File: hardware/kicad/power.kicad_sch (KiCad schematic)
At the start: 82 parts, among them IC401 TPS51206DSQR, U401 TPS62130ARGTR, U402 TPS62130ARGTR, U404 SPX3819M5-L-3-3, U405 TPS62130ARGTR

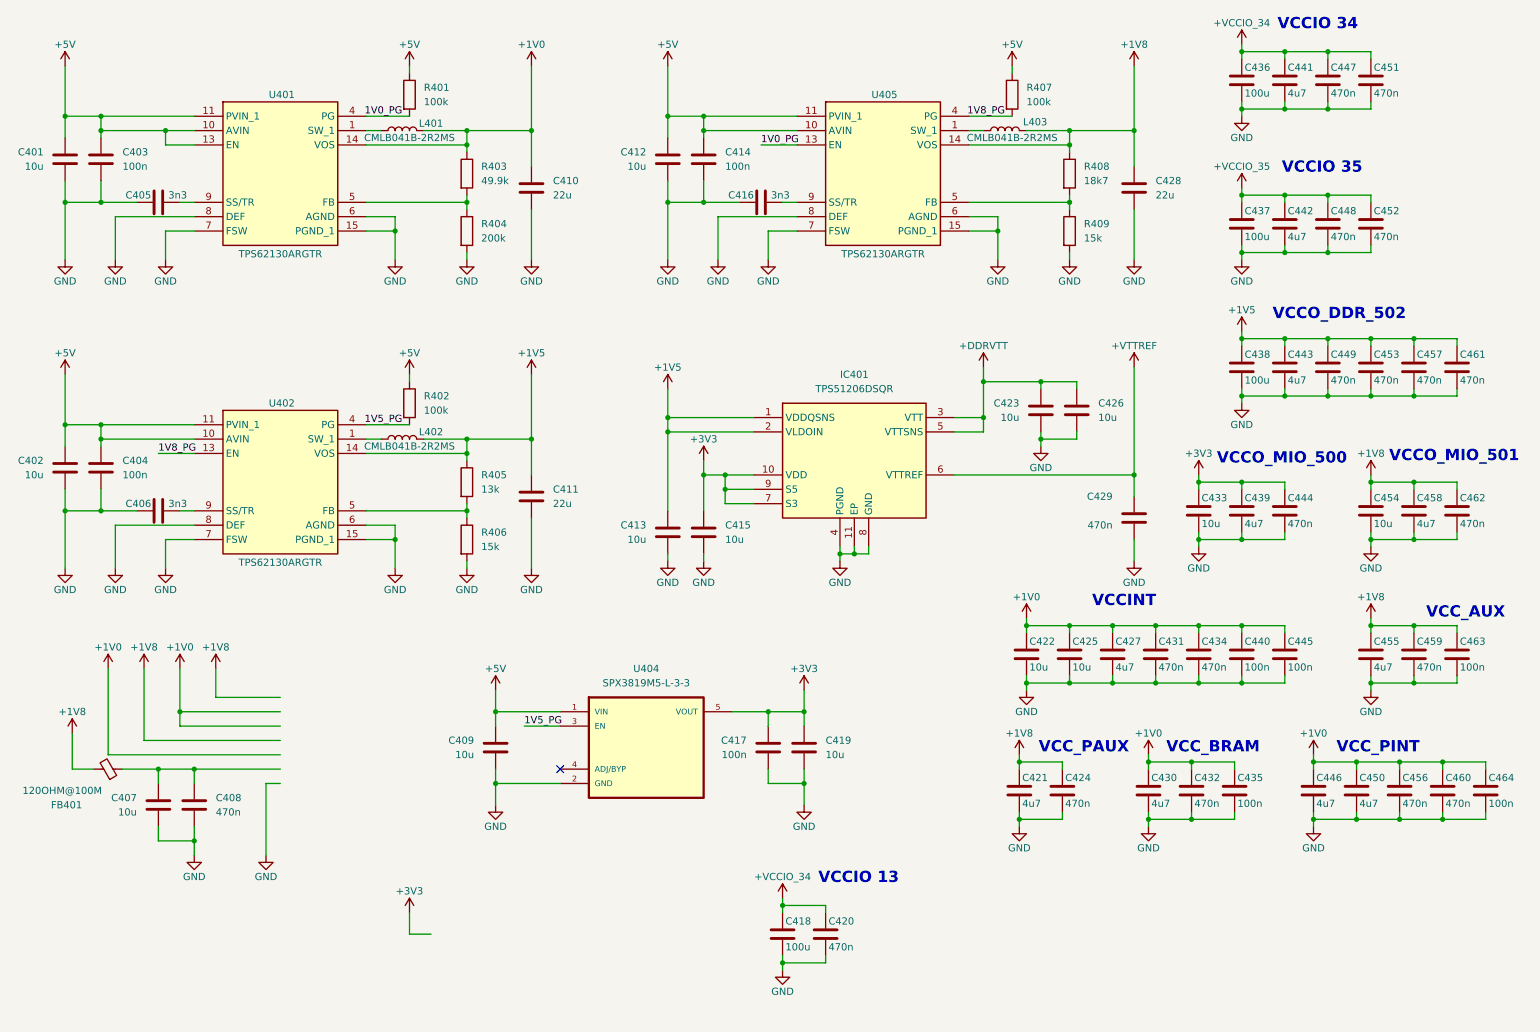
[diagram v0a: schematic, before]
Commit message: layout: finish dq0 & dq1 routing
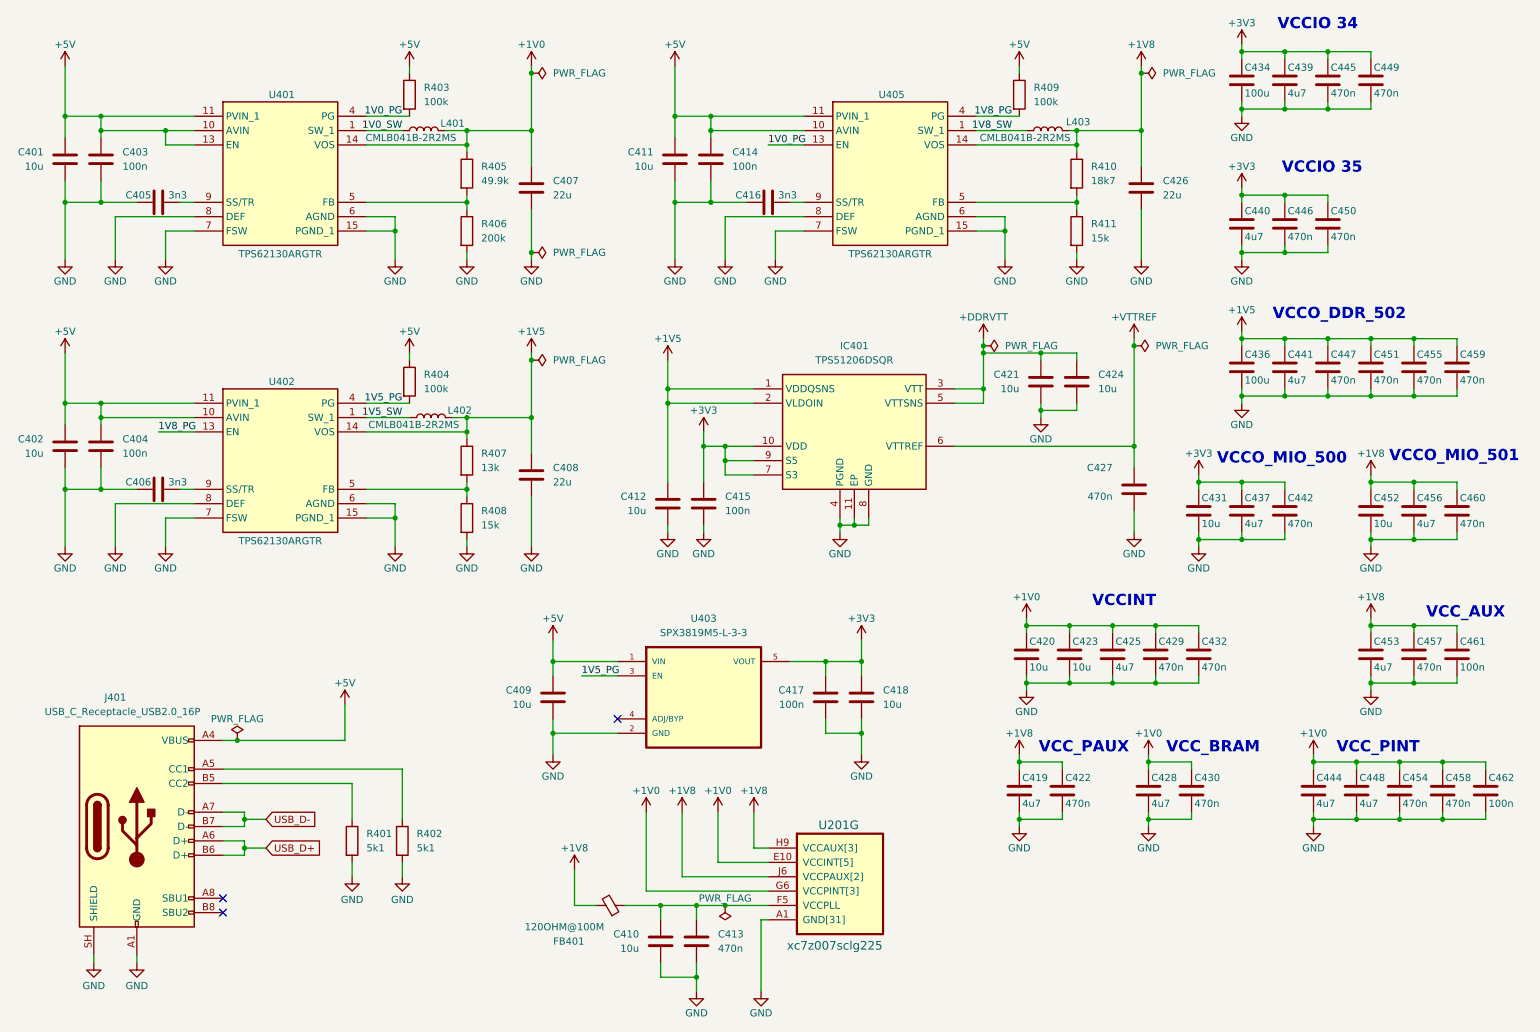
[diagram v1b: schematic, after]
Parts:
- removed C407: 10u, Capacitor_SMD:C_0805_2012Metric, symbol Device:C
- removed C408, C420: 470n, Capacitor_SMD:C_0402_1005Metric, symbol Device:C
- removed C418, C437: 100u, Capacitor_SMD:C_1206_3216Metric, symbol Device:C
- removed C435, C440, C445: 100n, Capacitor_SMD:C_0402_1005Metric, symbol Device:C
- added C410: 10u, Capacitor_SMD:C_0603_1608Metric, symbol Device:C
- added C413: 470n, Capacitor_SMD:C_0402_1005Metric, symbol Device:C
- added J401: USB_C_Receptacle_USB2.0_16P, Connector_USB:USB_C_Receptacle_GCT_USB4105-xx-A_16P_TopMnt_Horizontal, symbol Connector:USB_C_Receptacle_USB2.0_16P
- added R401, R402: 5k1, Resistor_SMD:R_0402_1005Metric, symbol Device:R
- added U201: xc7z007sclg225, Package_BGA:Xilinx_CLG225, symbol Xilinx7:xc7z007sclg225
- C415: value 10u -> 100n; footprint Capacitor_SMD:C_0805_2012Metric -> Capacitor_SMD:C_0402_1005Metric
- U403: renamed from U404; PACKAGE (none) -> SOT-23-5
- renumbered C410 to C407, C411 to C408, C412 to C411, C413 to C412, C419 to C418, C421 to C419, C422 to C420, C423 to C421, C424 to C422, C425 to C423, C426 to C424, C427 to C425, C428 to C426, C429 to C427, C430 to C428, C431 to C429, C432 to C430, C433 to C431, C434 to C432, C436 to C434, C438 to C436, C439 to C437, C441 to C439, C442 to C440, C443 to C441, C444 to C442, C446 to C444, C447 to C445, C448 to C446, C449 to C447, C450 to C448, C451 to C449, C452 to C450, C453 to C451, C454 to C452, C455 to C453, C456 to C454, C457 to C455, C458 to C456, C459 to C457, C460 to C458, C461 to C459, C462 to C460, C463 to C461, C464 to C462, R401 to R403, R402 to R404, R403 to R405, R404 to R406, R405 to R407, R406 to R408, R407 to R409, R408 to R410, R409 to R411
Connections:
- net +VCCIO_34 is gone; now on net +3V3: C434.1, C439.1, C445.1, C449.1
- net +VCCIO_35 is gone; now on net +3V3: C440.1, C446.1, C450.1
- net +1V0: now also U201.E10 (VCCINT[5]), U201.F9 (VCCINT[5]), U201.G10 (VCCINT[5]), U201.G6 (VCCPINT[3]), U201.H5 (VCCPINT[3]), U201.J10 (VCCINT[5]), U201.K5 (VCCPINT[3]), U201.L10 (VCCINT[5])
- net +1V8: now also U201.H9 (VCCAUX[3]), U201.J6 (VCCPAUX[2]), U201.J8 (VCCAUX[3]), U201.K9 (VCCAUX[3]), U201.L6 (VCCPAUX[2])
- net +5V: now also J401.A4 (VBUS), J401.A9 (VBUS), J401.B4 (VBUS), J401.B9 (VBUS)
- net GND: now also C410.2, C413.2, J401.A1 (GND), J401.A12 (GND), J401.B1 (GND), J401.B12 (GND), J401.SH (SHIELD), R401.2, R402.2, U201.A1 (GND[31]), U201.A11 (GND[31]), U201.B8 (GND[31]), U201.C15 (GND[31]), U201.C5 (GND[31]), U201.D12 (GND[31]), U201.D2 (GND[31]), U201.E5 (GND[31]), U201.E7 (GND[31]), U201.E9 (GND[31]), U201.F10 (GND[31]), U201.G13 (GND[31]), U201.G3 (GND[31]), U201.G5 (GND[31]), U201.H10 (GND[31]), U201.H6 (GND[31]), U201.J5 (GND[31]), U201.J9 (GND[31]), U201.K10 (GND[31]), U201.K14 (GND[31]), U201.K4 (GND[31]), U201.K7 (GND[31]), U201.L1 (GND[31]), U201.L11 (GND[31]), U201.L5 (GND[31]), U201.M8 (GND[31]), U201.N15 (GND[31]), U201.N5 (GND[31]), U201.P12 (GND[31]), U201.P2 (GND[31]), U201.R9 (GND[31])
- net at FB401.1: now also C410.1, C413.1, U201.F5 (VCCPLL)
- net 1V0_SW: now reaches L401.1, U401.1 (SW_1), U401.2 (SW_2), U401.3 (SW_3)
- net 1V8_SW: now reaches L403.1, U405.1 (SW_1), U405.2 (SW_2), U405.3 (SW_3)
- net 1V5_SW: now reaches L402.1, U402.1 (SW_1), U402.2 (SW_2), U402.3 (SW_3)
- new net: J401.B5 (CC2), R401.1
- new net: J401.A5 (CC1), R402.1
- new net USB_D+: J401.A6 (D+), J401.B6 (D+)
- new net USB_D-: J401.A7 (D-), J401.B7 (D-)
- no-connect marks 1 -> 3
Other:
- note removed: "VCCIO 13"
- moved on the sheet: C402, C404, C406, C408, C409, C411, C412, C414, C415, C416, C417, C418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

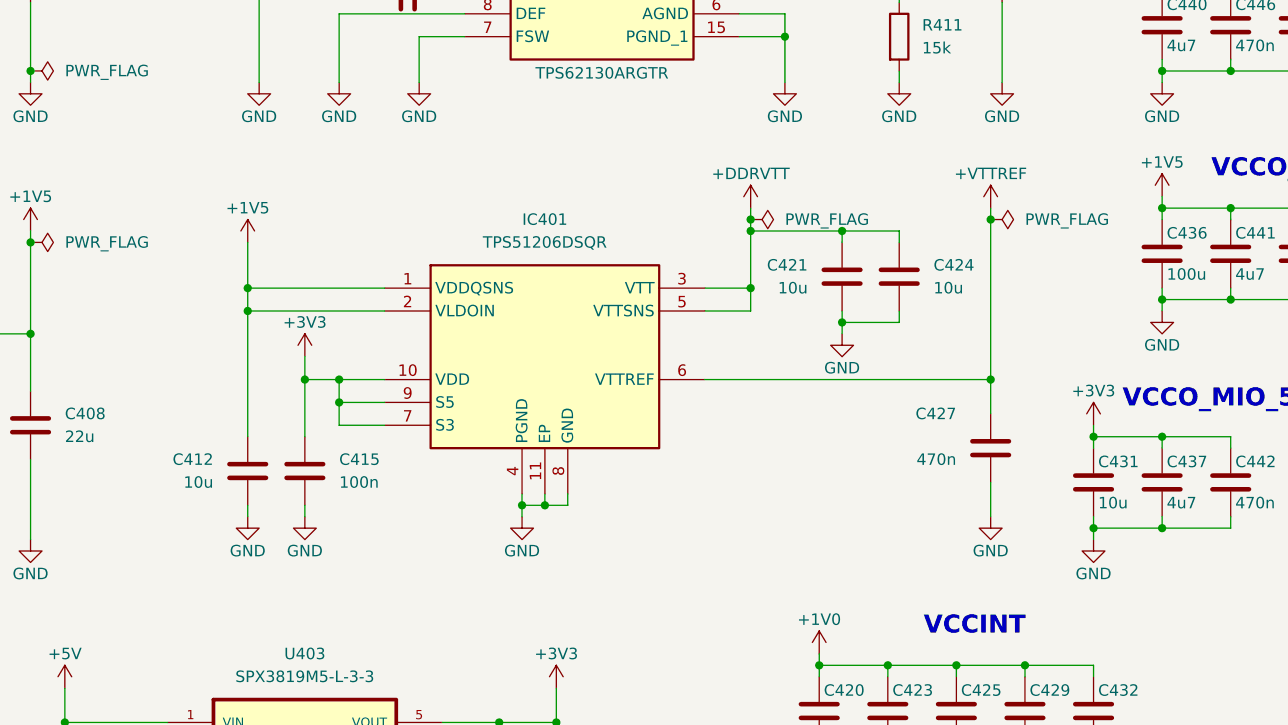
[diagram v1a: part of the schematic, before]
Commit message: pcb: complete FPGA and DDR BGA breakout
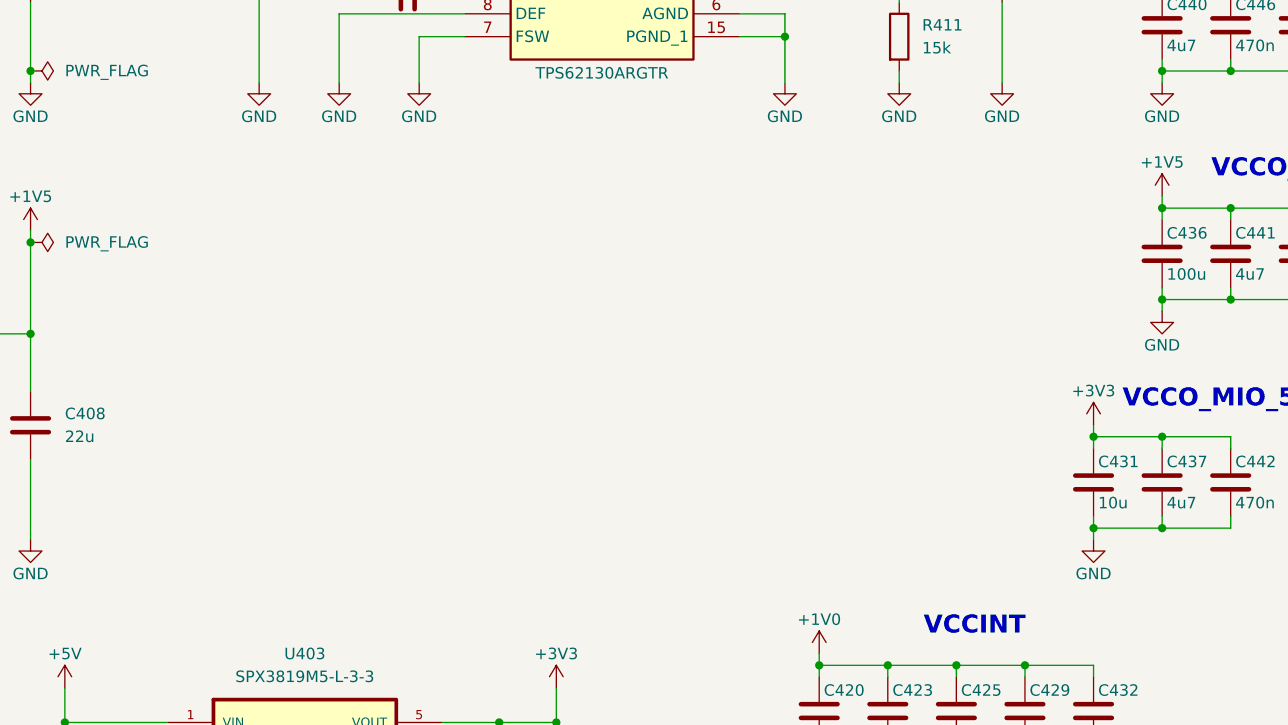
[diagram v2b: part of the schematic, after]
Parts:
- removed C412, C421, C424: 10u, Capacitor_SMD:C_0805_2012Metric, symbol Device:C
- removed C415: 100n, Capacitor_SMD:C_0402_1005Metric, symbol Device:C
- removed C427: 470n, Capacitor_SMD:C_0402_1005Metric, symbol Device:C
- removed IC401: TPS51206DSQR, Project:SON40P200X200X80-11N, symbol TPS51206DSQR:TPS51206DSQR

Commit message: feat: need switch two singals of SD inferface
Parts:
- C401, C402, C407, C408, C409, C411, C418, C420, C423, C426, C431, C452: footprint Capacitor_SMD:C_0805_2012Metric -> Capacitor_SMD:C_0603_1608Metric
- R401, R402: footprint Resistor_SMD:R_0402_1005Metric -> Resistor_SMD:R_0603_1608Metric
- U201: footprint Package_BGA:Xilinx_CLG225 -> (none)
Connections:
- net USB_D+: no longer names the net of J401.A6 (D+)
- net USB_D+: no longer J401.B6 (D+)
- net USB_D-: no longer names the net of J401.A7 (D-)
- net USB_D-: no longer J401.B7 (D-)
- no-connect marks 3 -> 7
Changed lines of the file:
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@@
 	)
 	(junction
-		(at 57.15 158.75)
-		(diameter 0)
-		(color 0 0 0 0)
-	)
-	(junction
 		(at 261.62 158.75)
 		(diameter 0)
@@
 	)
 	(junction
-		(at 57.15 163.83)
-		(diameter 0)
-		(color 0 0 0 0)
-	)
-	(junction
 		(at 31.75 49.53)
 		(diameter 0)
@@
 	)
 	(no_connect
+		(at 53.34 157.48)
+	)
+	(no_connect
 		(at 123.19 140.97)
 	)
@@
 	)
 	(no_connect
+		(at 53.34 160.02)
+	)
+	(no_connect
+		(at 53.34 165.1)
+	)
+	(no_connect
+		(at 53.34 162.56)
+	)
+	(no_connect
 		(at 53.34 172.72)
 	)
@@
 	(wire
 		(pts
-			(xy 57.15 163.83) (xy 60.96 163.83)
-		)
-		(stroke
-			(width 0)
-			(type default)
-		)
-	)
-	(wire
-		(pts
 			(xy 78.74 87.63) (xy 86.36 87.63)
 		)
@@
 	(wire
 		(pts
-			(xy 53.34 160.02) (xy 57.15 160.02)
-		)
-		(stroke
-			(width 0)
-			(type default)
-		)
-	)
-	(wire
-		(pts
 			(xy 130.81 184.15) (xy 130.81 186.69)
 		)
@@
 	(wire
 		(pts
-			(xy 57.15 158.75) (xy 57.15 160.02)
-		)
-		(stroke
-			(width 0)
-			(type default)
-		)
-	)
-	(wire
-		(pts
 			(xy 96.52 87.63) (xy 96.52 90.17)
 		)
@@
 	(wire
 		(pts
-			(xy 57.15 162.56) (xy 57.15 163.83)
-		)
-		(stroke
-			(width 0)
-			(type default)
-		)
-	)
-	(wire
-		(pts
 			(xy 78.74 90.17) (xy 96.52 90.17)
 		)
@@
 	(wire
 		(pts
-			(xy 53.34 157.48) (xy 57.15 157.48)
-		)
-		(stroke
-			(width 0)
-			(type default)
-		)
-	)
-	(wire
-		(pts
 			(xy 204.47 50.8) (xy 204.47 49.53)
 		)
@@
 	(wire
 		(pts
-			(xy 57.15 163.83) (xy 57.15 165.1)
-		)
-		(stroke
-			(width 0)
-			(type default)
-		)
-	)
-	(wire
-		(pts
-			(xy 53.34 162.56) (xy 57.15 162.56)
-		)
-		(stroke
-			(width 0)
-			(type default)
-		)
-	)
-	(wire
-		(pts
 			(xy 248.92 33.02) (xy 241.3 33.02)
 		)
@@
 	(wire
 		(pts
-			(xy 57.15 158.75) (xy 60.96 158.75)
-		)
-		(stroke
-			(width 0)
-			(type default)
-		)
-	)
-	(wire
-		(pts
 			(xy 241.3 58.42) (xy 233.68 58.42)
 		)
@@
 	(wire
 		(pts
-			(xy 57.15 157.48) (xy 57.15 158.75)
-		)
-		(stroke
-			(width 0)
-			(type default)
-		)
-	)
-	(wire
-		(pts
 			(xy 248.92 22.86) (xy 256.54 22.86)
 		)
@@
 	(wire
 		(pts
-			(xy 53.34 165.1) (xy 57.15 165.1)
-		)
-		(stroke
-			(width 0)
-			(type default)
-		)
-	)
-	(wire
-		(pts
 			(xy 148.59 189.23) (xy 148.59 176.53)
 		)
@@
 		)
 	)
-	(global_label "USB_D+"
-		(shape input)
-		(at 60.96 163.83 0)
-		(fields_autoplaced yes)
-		(effects
-			(font
-				(size 1.27 1.27)
-			)
-			(justify left)
-		)
-		(property "Intersheetrefs" "${INTERSHEET_REFS}"
-			(at 71.5652 163.83 0)
-			(hide yes)
-			(show_name no)
-			(do_not_autoplace no)
-			(effects
-				(font
-					(size 1.27 1.27)
-				)
-				(justify left)
-			)
-		)
-	)
-	(global_label "USB_D-"
-		(shape input)
-		(at 60.96 158.75 0)
-		(fields_autoplaced yes)
-		(effects
-			(font
-				(size 1.27 1.27)
-			)
-			(justify left)
-		)
-		(property "Intersheetrefs" "${INTERSHEET_REFS}"
-			(at 71.5652 158.75 0)
-			(hide yes)
-			(show_name no)
-			(do_not_autoplace no)
-			(effects
-				(font
-					(size 1.27 1.27)
-				)
-				(justify left)
-			)
-		)
-	)
 	(rule_area
 		(exclude_from_sim no)
@@
 			)
 		)
-		(property "Footprint" "Resistor_SMD:R_0402_1005Metric"
+		(property "Footprint" "Resistor_SMD:R_0603_1608Metric"
 			(at 74.422 162.56 90)
 			(hide yes)
@@
 			)
 		)
-		(property "Footprint" "Capacitor_SMD:C_0805_2012Metric"
+		(property "Footprint" "Capacitor_SMD:C_0603_1608Metric"
 			(at 24.4348 96.52 0)
 			(hide yes)
@@
 			)
 		)
-		(property "Footprint" "Capacitor_SMD:C_0805_2012Metric"
+		(property "Footprint" "Capacitor_SMD:C_0603_1608Metric"
 			(at 24.4348 45.72 0)
 			(hide yes)
@@
 			)
 		)
-		(property "Footprint" "Capacitor_SMD:C_0805_2012Metric"
+		(property "Footprint" "Capacitor_SMD:C_0603_1608Metric"
 			(at 108.9152 101.6 0)
 			(hide yes)
@@
 			)
 		)
-		(property "Footprint" "Capacitor_SMD:C_0805_2012Metric"
+		(property "Footprint" "Capacitor_SMD:C_0603_1608Metric"
 			(at 132.3848 45.72 0)
 			(hide yes)
@@
 			)
 		)
-		(property "Footprint" "Capacitor_SMD:C_0805_2012Metric"
+		(property "Footprint" "Capacitor_SMD:C_0603_1608Metric"
 			(at 227.0252 107.95 0)
 			(hide yes)
@@
 			)
 		)
-		(property "Footprint" "Capacitor_SMD:C_0805_2012Metric"
+		(property "Footprint" "Capacitor_SMD:C_0603_1608Metric"
 			(at 257.5052 107.95 0)
 			(hide yes)
@@
 			)
 		)
-		(property "Footprint" "Capacitor_SMD:C_0805_2012Metric"
+		(property "Footprint" "Capacitor_SMD:C_0603_1608Metric"
 			(at 110.7948 140.97 0)
 			(hide yes)
@@
 			)
 		)
-		(property "Footprint" "Capacitor_SMD:C_0805_2012Metric"
+		(property "Footprint" "Capacitor_SMD:C_0603_1608Metric"
 			(at 204.1652 133.35 0)
 			(hide yes)
@@
 			)
 		)
-		(property "Footprint" "Capacitor_SMD:C_0805_2012Metric"
+		(property "Footprint" "Capacitor_SMD:C_0603_1608Metric"
 			(at 216.8652 50.8 0)
 			(hide yes)
@@
 			)
 		)
-		(property "Footprint" "Capacitor_SMD:C_0805_2012Metric"
+		(property "Footprint" "Capacitor_SMD:C_0603_1608Metric"
 			(at 167.3352 140.97 0)
 			(hide yes)
@@
 			)
 		)
-		(property "Footprint" "Resistor_SMD:R_0402_1005Metric"
+		(property "Footprint" "Resistor_SMD:R_0603_1608Metric"
 			(at 83.312 162.56 90)
 			(hide yes)
@@
 			)
 		)
-		(property "Footprint" "Package_BGA:Xilinx_CLG225"
+		(property "Footprint" ""
 			(at 154.94 162.56 0)
 			(hide yes)
@@
 			)
 		)
-		(property "Footprint" "Capacitor_SMD:C_0805_2012Metric"
+		(property "Footprint" "Capacitor_SMD:C_0603_1608Metric"
 			(at 196.5452 133.35 0)
 			(hide yes)
@@
 			)
 		)
-		(property "Footprint" "Capacitor_SMD:C_0805_2012Metric"
+		(property "Footprint" "Capacitor_SMD:C_0603_1608Metric"
 			(at 108.9152 50.8 0)
 			(hide yes)
